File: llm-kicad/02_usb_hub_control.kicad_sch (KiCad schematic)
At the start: 23 parts, among them J1 TYPE-C-31-M-12, Q6 BSS138P,215, Q7 BSS138P,215, U1 CH334F, U2 CP2102N-A02-GQFN28, U9 TPD4E05U06DQA, Y1 Crystal 12MHz

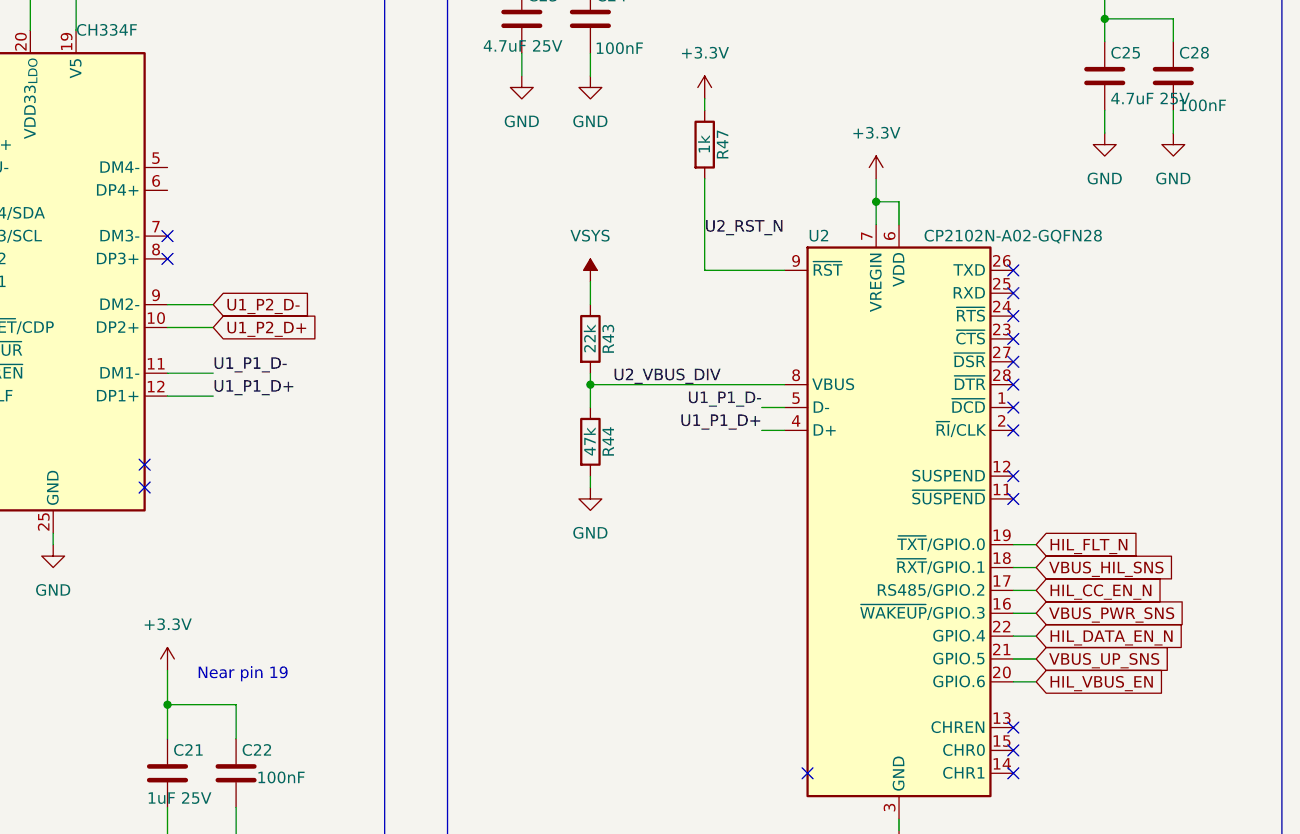
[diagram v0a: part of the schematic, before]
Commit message: Fixed incorrect footprint and added external GPIO
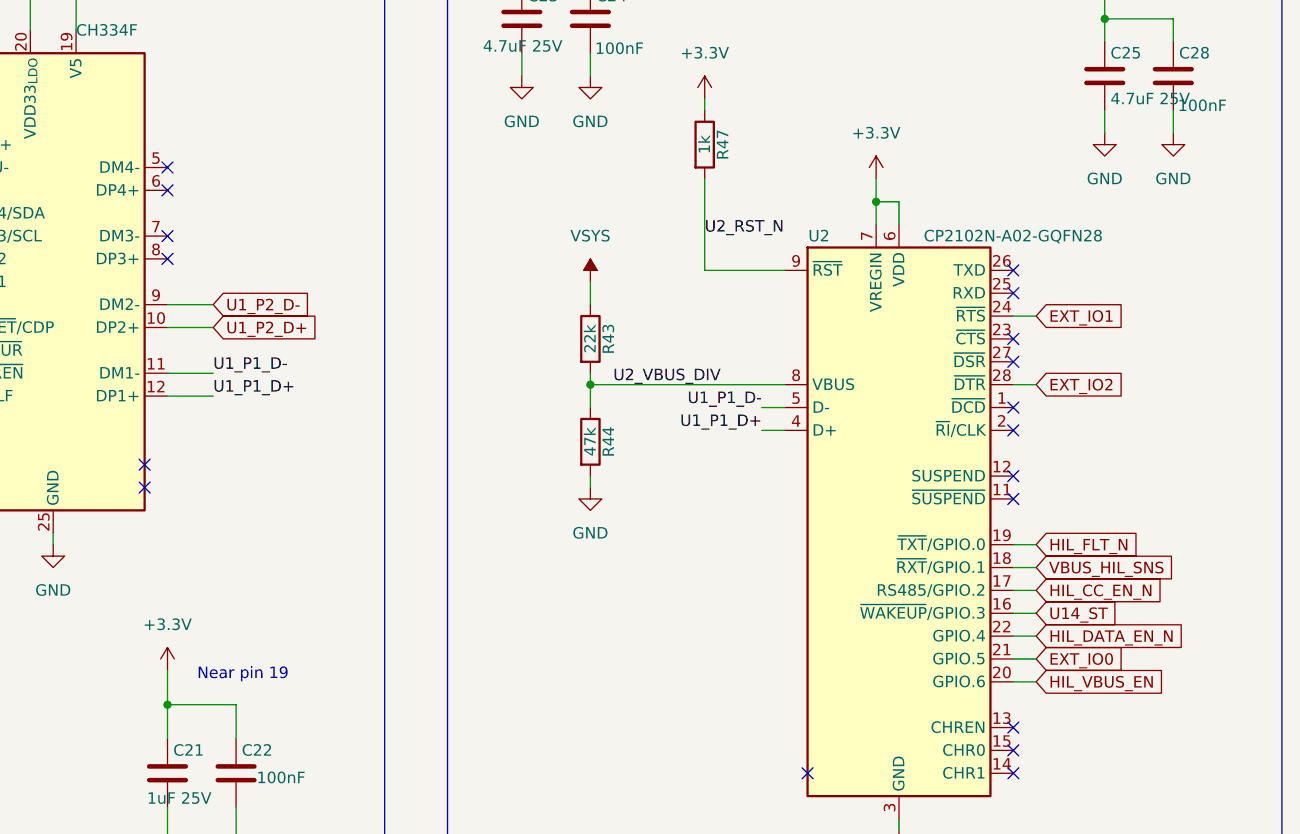
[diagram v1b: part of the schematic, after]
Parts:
- U1: footprint Package_DFN_QFN:QFN-24-1EP_4x4mm_P0.5mm_EP2.6x2.6mm_ThermalVias -> Package_DFN_QFN:QFN-24-1EP_4x4mm_P0.5mm_EP2.7x2.7mm
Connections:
- net EXT_IO1: now reaches U2.24 (~{RTS})
- net EXT_IO2: now reaches U2.28 (~{DTR})
- net VBUS_PWR_SNS renamed U14_ST
- net VBUS_UP_SNS renamed EXT_IO0
